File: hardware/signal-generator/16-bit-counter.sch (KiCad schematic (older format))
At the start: 8 parts, among them U1 74HC04, U13 74HC4040, U14 74HC4040, U2 74HC08, U3 74HC08, U4 74HC30

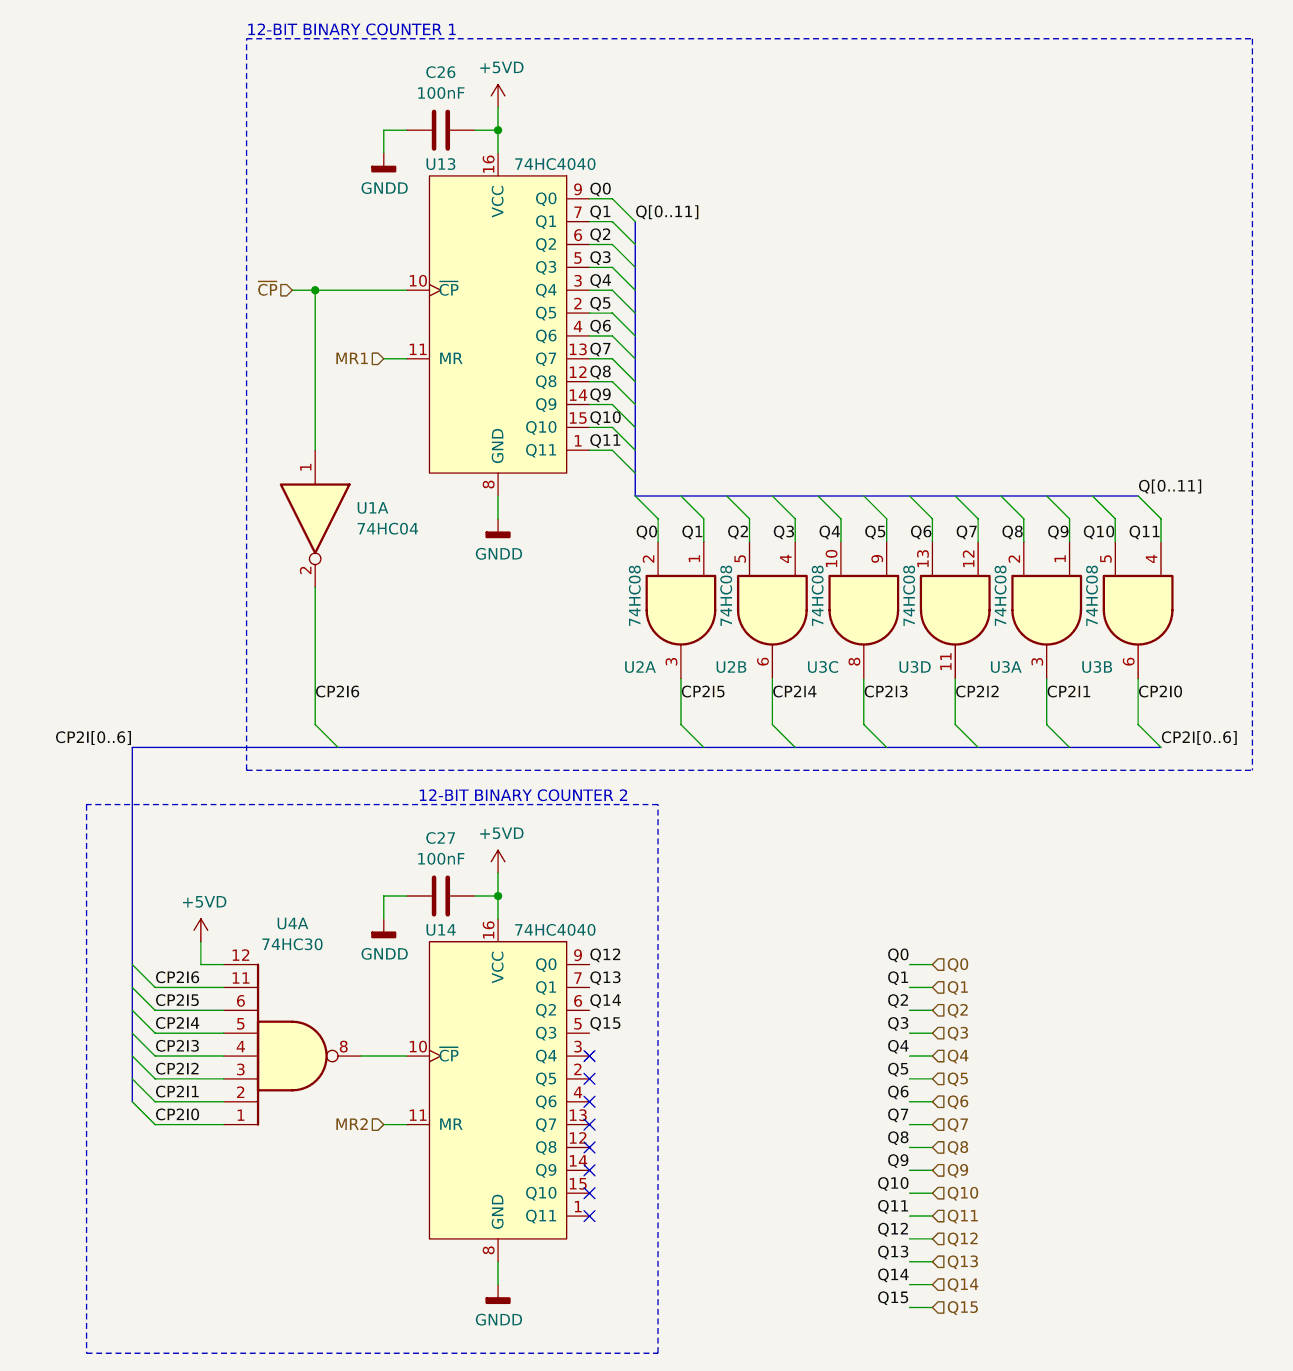
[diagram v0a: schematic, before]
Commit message: [Signal Generator] Change LCD backlight control method
The LCD's backlight was previously intended to be controlled via a
digital potentiometer. However, a much more elegant solution is to
control said backlight via PWM.

Also, removed the level shifter schematic sheet. The level shifters have been
moved to the TFT module's schematic sheet.
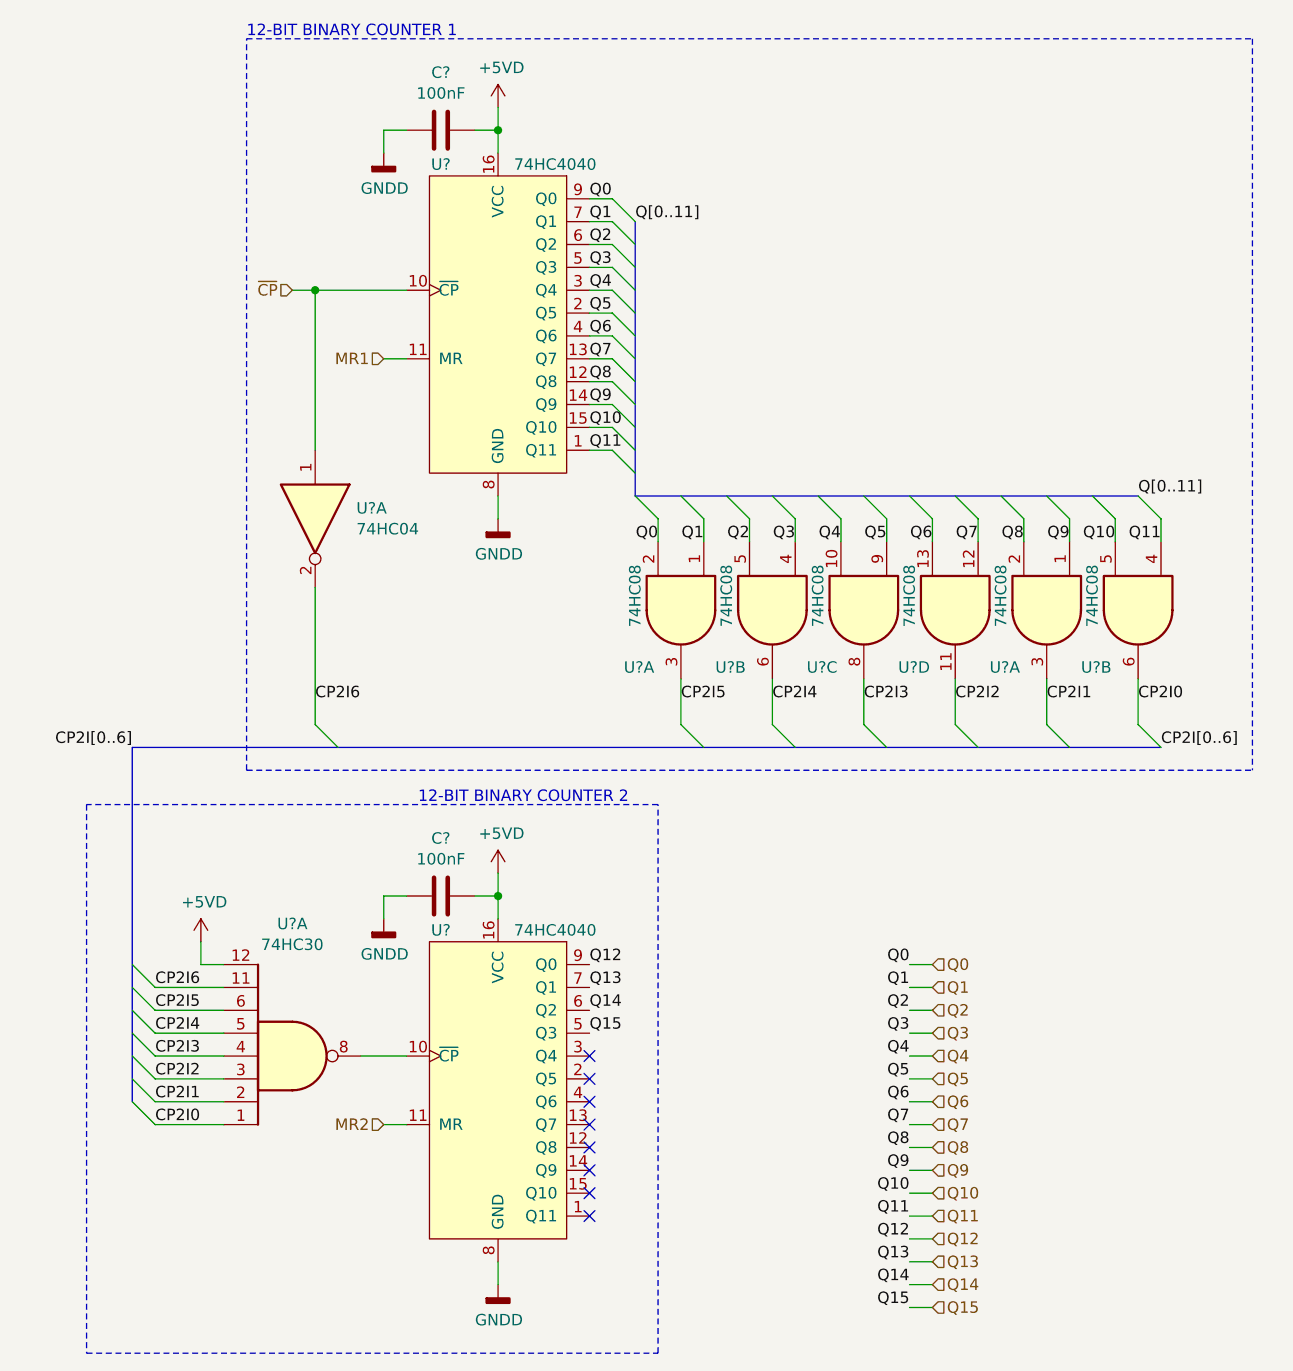
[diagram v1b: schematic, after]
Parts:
- renumbered C27 to C?, C26 to C?, U1 to U?, U13 to U?, U14 to U?, U4 to U?, U2 to U?, U3 to U?
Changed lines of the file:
@@
 $Descr A4 11693 8268
 encoding utf-8
-Sheet 3 6
+Sheet 3 5
 Title "Digital Function Generator v2 - DDS 16-bit counter"
 Date "2019-12-02"
@@
 	3650 5300 3850 5300
 $Comp
-L Device:C C27
+L Device:C C?
 U 1 1 5DBB7F3D
 P 4000 4600
-F 0 "C27" V 3748 4600 50  0000 C CNN
+F 0 "C?" V 3748 4600 50  0000 C CNN
 F 1 "100nF" V 3839 4600 50  0000 C CNN
 F 2 "Capacitors_SMD:C_0805_HandSoldering" H 4038 4450 50  0001 C CNN
@@
 	3750 4600 3750 4700
 $Comp
-L power:GNDD #PWR0172
+L power:GNDD #PWR?
 U 1 1 5DBB9690
 P 3750 4700
-F 0 "#PWR0172" H 3750 4450 50  0001 C CNN
+F 0 "#PWR?" H 3750 4450 50  0001 C CNN
 F 1 "GNDD" H 3754 4545 50  0000 C CNN
 F 2 "" H 3750 4700 50  0001 C CNN
@@
 Connection ~ 4250 4600
 $Comp
-L power:+5VD #PWR0173
+L power:+5VD #PWR?
 U 1 1 5DBB9DC1
 P 4250 4500
-F 0 "#PWR0173" H 4250 4350 50  0001 C CNN
+F 0 "#PWR?" H 4250 4350 50  0001 C CNN
 F 1 "+5VD" H 4265 4673 50  0000 C CNN
 F 2 "" H 4250 4500 50  0001 C CNN
@@
 $EndComp
 $Comp
-L Device:C C26
+L Device:C C?
 U 1 1 5DBBA88D
 P 4000 1250
-F 0 "C26" V 3748 1250 50  0000 C CNN
+F 0 "C?" V 3748 1250 50  0000 C CNN
 F 1 "100nF" V 3839 1250 50  0000 C CNN
 F 2 "Capacitors_SMD:C_0805_HandSoldering" H 4038 1100 50  0001 C CNN
@@
 	3750 1250 3750 1350
 $Comp
-L power:GNDD #PWR0174
+L power:GNDD #PWR?
 U 1 1 5DBBB94E
 P 3750 1350
-F 0 "#PWR0174" H 3750 1100 50  0001 C CNN
+F 0 "#PWR?" H 3750 1100 50  0001 C CNN
 F 1 "GNDD" H 3754 1195 50  0000 C CNN
 F 2 "" H 3750 1350 50  0001 C CNN
@@
 Connection ~ 4250 1250
 $Comp
-L power:+5VD #PWR0175
+L power:+5VD #PWR?
 U 1 1 5DBBC2D6
 P 4250 1150
-F 0 "#PWR0175" H 4250 1000 50  0001 C CNN
+F 0 "#PWR?" H 4250 1000 50  0001 C CNN
 F 1 "+5VD" H 4265 1323 50  0000 C CNN
 F 2 "" H 4250 1150 50  0001 C CNN
@@
 	4250 2850 4250 2950
 $Comp
-L power:GNDD #PWR0176
+L power:GNDD #PWR?
 U 1 1 5DBBD1F3
 P 4250 2950
-F 0 "#PWR0176" H 4250 2700 50  0001 C CNN
+F 0 "#PWR?" H 4250 2700 50  0001 C CNN
 F 1 "GNDD" H 4254 2795 50  0000 C CNN
 F 2 "" H 4250 2950 50  0001 C CNN
@@
 	4250 6200 4250 6300
 $Comp
-L power:GNDD #PWR0177
+L power:GNDD #PWR?
 U 1 1 5DBBE1A2
 P 4250 6300
-F 0 "#PWR0177" H 4250 6050 50  0001 C CNN
+F 0 "#PWR?" H 4250 6050 50  0001 C CNN
 F 1 "GNDD" H 4254 6145 50  0000 C CNN
 F 2 "" H 4250 6300 50  0001 C CNN
@@
 	2950 4900 2950 4800
 $Comp
-L power:+5VD #PWR0178
+L power:+5VD #PWR?
 U 1 1 5DBCA96D
 P 2950 4800
-F 0 "#PWR0178" H 2950 4650 50  0001 C CNN
+F 0 "#PWR?" H 2950 4650 50  0001 C CNN
 F 1 "+5VD" H 2965 4973 50  0000 C CNN
 F 2 "" H 2950 4800 50  0001 C CNN
@@
 12-BIT BINARY COUNTER 2
 $Comp
-L 74xx:74HC04 U1
+L 74xx:74HC04 U?
 U 1 1 5DBD607E
 P 3450 2950
-F 0 "U1" V 3404 3130 50  0000 L CNN
+F 0 "U?" V 3404 3130 50  0000 L CNN
 F 1 "74HC04" V 3495 3130 50  0000 L CNN
 F 2 "Housings_SOIC:SOIC-14_3.9x8.7mm_Pitch1.27mm" H 3450 2950 50  0001 C CNN
@@
 	3450 1950 3850 1950
 $Comp
-L ulib_MY_74xx:74HC4040 U13
+L ulib_MY_74xx:74HC4040 U?
 U 1 1 5DDE79E4
 P 4250 2100
-F 0 "U13" H 4000 2800 50  0000 C CNN
+F 0 "U?" H 4000 2800 50  0000 C CNN
 F 1 "74HC4040" H 4500 2800 50  0000 C CNN
 F 2 "Housings_SOIC:SOIC-16_3.9x9.9mm_Pitch1.27mm" H 4250 2050 50  0001 C CNN
@@
 $EndComp
 $Comp
-L ulib_MY_74xx:74HC4040 U14
+L ulib_MY_74xx:74HC4040 U?
 U 1 1 5DDE7D79
 P 4250 5450
-F 0 "U14" H 4000 6150 50  0000 C CNN
+F 0 "U?" H 4000 6150 50  0000 C CNN
 F 1 "74HC4040" H 4500 6150 50  0000 C CNN
 F 2 "Housings_SOIC:SOIC-16_3.9x9.9mm_Pitch1.27mm" H 4250 5400 50  0001 C CNN
@@
 $EndComp
 $Comp
-L ulib_MY_74xx:74HC30 U4
+L ulib_MY_74xx:74HC30 U?
 U 1 1 5DDE81EA
 P 3350 5300
-F 0 "U4" H 3350 4722 50  0000 C CNN
+F 0 "U?" H 3350 4722 50  0000 C CNN
 F 1 "74HC30" H 3350 4813 50  0000 C CNN
 F 2 "Housings_SOIC:SOIC-14_3.9x8.7mm_Pitch1.27mm" H 3350 5250 50  0001 C CNN
@@
 $EndComp
 $Comp
-L ulib_MY_74xx:74HC08 U2
+L ulib_MY_74xx:74HC08 U?
 U 1 1 5DDE88D1
 P 5050 3350
-F 0 "U2" V 5300 3100 50  0000 L CNN
+F 0 "U?" V 5300 3100 50  0000 L CNN
 F 1 "74HC08" H 4850 3150 50  0000 L CNN
 F 2 "Housings_SOIC:SOIC-14_3.9x8.7mm_Pitch1.27mm" H 5050 3300 50  0001 C CNN
@@
 $EndComp
 $Comp
-L ulib_MY_74xx:74HC08 U2
+L ulib_MY_74xx:74HC08 U?
 U 2 1 5DDE89F7
 P 5450 3350
-F 0 "U2" V 5700 3100 50  0000 L CNN
+F 0 "U?" V 5700 3100 50  0000 L CNN
 F 1 "74HC08" H 5250 3150 50  0000 L CNN
 F 2 "Housings_SOIC:SOIC-14_3.9x8.7mm_Pitch1.27mm" H 5450 3300 50  0001 C CNN
@@
 $EndComp
 $Comp
-L ulib_MY_74xx:74HC08 U3
+L ulib_MY_74xx:74HC08 U?
 U 3 1 5DDE8B26
 P 5850 3350
-F 0 "U3" V 6100 3100 50  0000 L CNN
+F 0 "U?" V 6100 3100 50  0000 L CNN
 F 1 "74HC08" H 5650 3150 50  0000 L CNN
 F 2 "Housings_SOIC:SOIC-14_3.9x8.7mm_Pitch1.27mm" H 5850 3300 50  0001 C CNN
@@
 $EndComp
 $Comp
-L ulib_MY_74xx:74HC08 U3
+L ulib_MY_74xx:74HC08 U?
 U 4 1 5DDE8C64
 P 6250 3350
-F 0 "U3" V 6500 3100 50  0000 L CNN
+F 0 "U?" V 6500 3100 50  0000 L CNN
 F 1 "74HC08" H 6050 3150 50  0000 L CNN
 F 2 "Housings_SOIC:SOIC-14_3.9x8.7mm_Pitch1.27mm" H 6250 3300 50  0001 C CNN
@@
 $EndComp
 $Comp
-L ulib_MY_74xx:74HC08 U3
+L ulib_MY_74xx:74HC08 U?
 U 1 1 5DDE8DB3
 P 6650 3350
-F 0 "U3" V 6900 3100 50  0000 L CNN
+F 0 "U?" V 6900 3100 50  0000 L CNN
 F 1 "74HC08" H 6450 3150 50  0000 L CNN
 F 2 "Housings_SOIC:SOIC-14_3.9x8.7mm_Pitch1.27mm" H 6650 3300 50  0001 C CNN
@@
 $EndComp
 $Comp
-L ulib_MY_74xx:74HC08 U3
+L ulib_MY_74xx:74HC08 U?
 U 2 1 5DDE8F14
 P 7050 3350
-F 0 "U3" V 7300 3100 50  0000 L CNN
+F 0 "U?" V 7300 3100 50  0000 L CNN
 F 1 "74HC08" H 6850 3150 50  0000 L CNN
 F 2 "Housings_SOIC:SOIC-14_3.9x8.7mm_Pitch1.27mm" H 7050 3300 50  0001 C CNN

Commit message: [Signal Generator] Finalize schematic
The electronic schematic is now finalized. All components have been
annotated. Furthermore, all components have an appropriate footprint
associated to them.
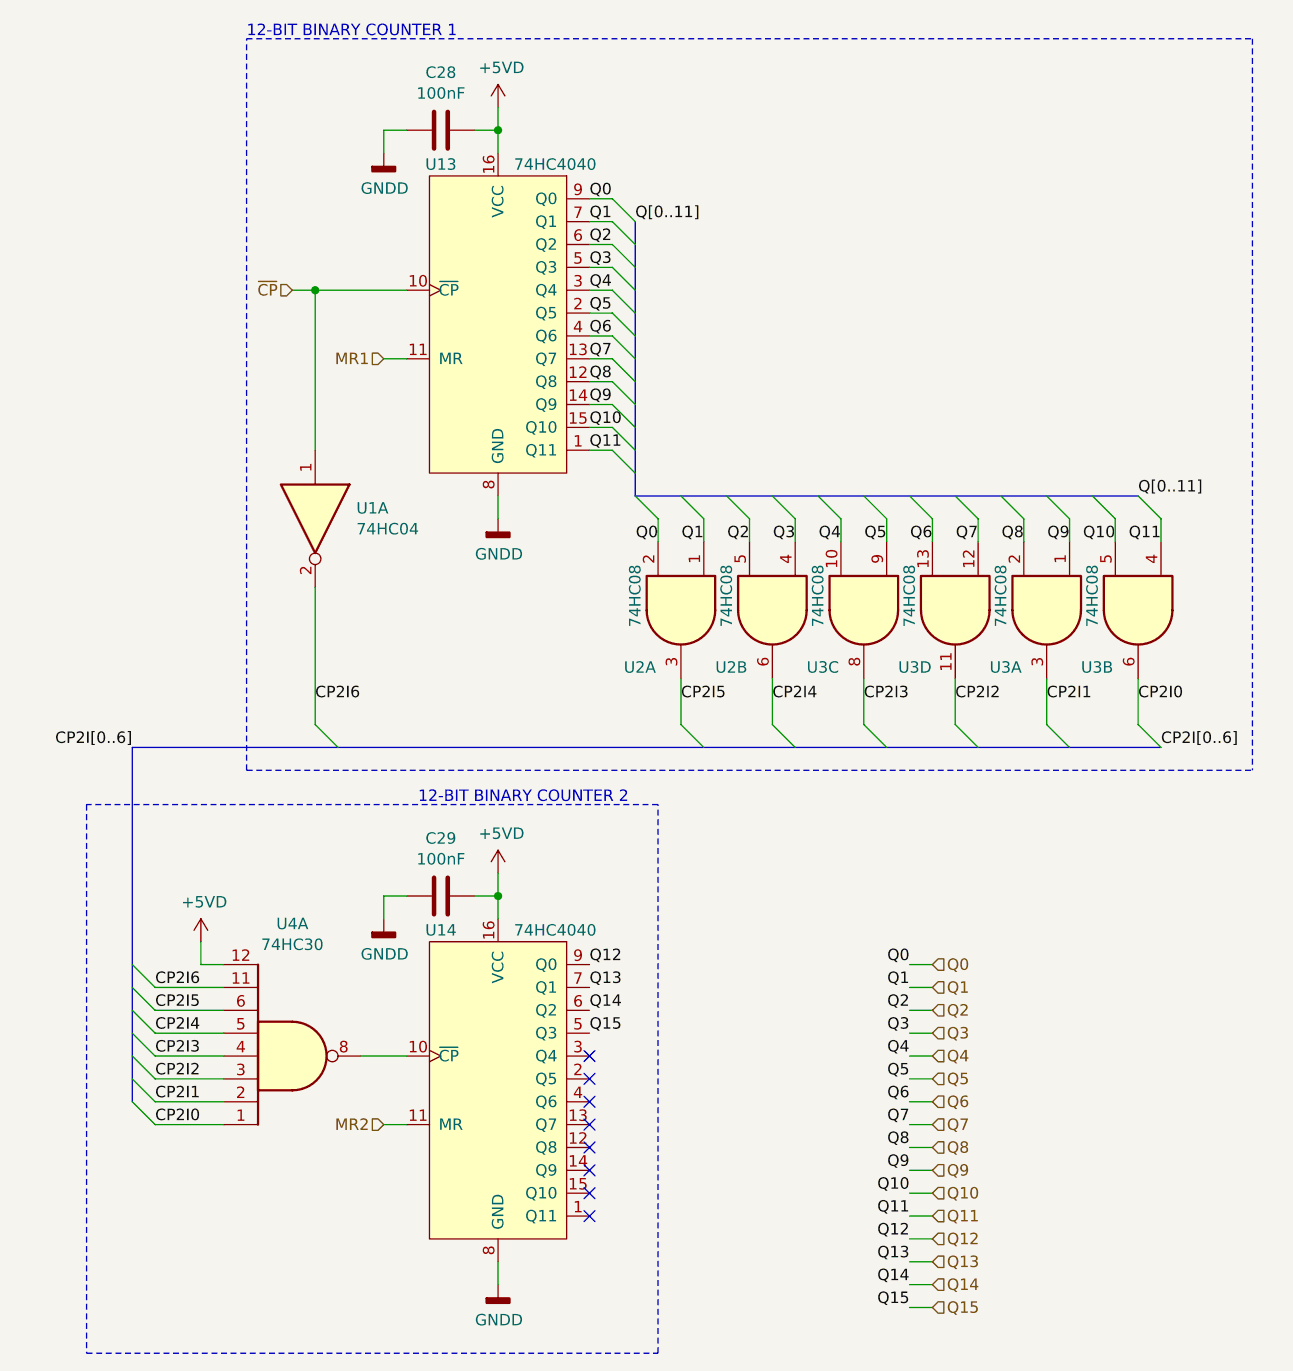
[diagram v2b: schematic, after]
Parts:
- gave numbers to parts that had none: 8
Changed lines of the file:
@@
 	3650 5300 3850 5300
 $Comp
-L Device:C C?
+L Device:C C29
 U 1 1 5DBB7F3D
 P 4000 4600
-F 0 "C?" V 3748 4600 50  0000 C CNN
+F 0 "C29" V 3748 4600 50  0000 C CNN
 F 1 "100nF" V 3839 4600 50  0000 C CNN
 F 2 "Capacitors_SMD:C_0805_HandSoldering" H 4038 4450 50  0001 C CNN
@@
 	3750 4600 3750 4700
 $Comp
-L power:GNDD #PWR?
+L power:GNDD #PWR077
 U 1 1 5DBB9690
 P 3750 4700
-F 0 "#PWR?" H 3750 4450 50  0001 C CNN
+F 0 "#PWR077" H 3750 4450 50  0001 C CNN
 F 1 "GNDD" H 3754 4545 50  0000 C CNN
 F 2 "" H 3750 4700 50  0001 C CNN
@@
 Connection ~ 4250 4600
 $Comp
-L power:+5VD #PWR?
+L power:+5VD #PWR080
 U 1 1 5DBB9DC1
 P 4250 4500
-F 0 "#PWR?" H 4250 4350 50  0001 C CNN
+F 0 "#PWR080" H 4250 4350 50  0001 C CNN
 F 1 "+5VD" H 4265 4673 50  0000 C CNN
 F 2 "" H 4250 4500 50  0001 C CNN
@@
 $EndComp
 $Comp
-L Device:C C?
+L Device:C C28
 U 1 1 5DBBA88D
 P 4000 1250
-F 0 "C?" V 3748 1250 50  0000 C CNN
+F 0 "C28" V 3748 1250 50  0000 C CNN
 F 1 "100nF" V 3839 1250 50  0000 C CNN
 F 2 "Capacitors_SMD:C_0805_HandSoldering" H 4038 1100 50  0001 C CNN
@@
 	3750 1250 3750 1350
 $Comp
-L power:GNDD #PWR?
+L power:GNDD #PWR076
 U 1 1 5DBBB94E
 P 3750 1350
-F 0 "#PWR?" H 3750 1100 50  0001 C CNN
+F 0 "#PWR076" H 3750 1100 50  0001 C CNN
 F 1 "GNDD" H 3754 1195 50  0000 C CNN
 F 2 "" H 3750 1350 50  0001 C CNN
@@
 Connection ~ 4250 1250
 $Comp
-L power:+5VD #PWR?
+L power:+5VD #PWR078
 U 1 1 5DBBC2D6
 P 4250 1150
-F 0 "#PWR?" H 4250 1000 50  0001 C CNN
+F 0 "#PWR078" H 4250 1000 50  0001 C CNN
 F 1 "+5VD" H 4265 1323 50  0000 C CNN
 F 2 "" H 4250 1150 50  0001 C CNN
@@
 	4250 2850 4250 2950
 $Comp
-L power:GNDD #PWR?
+L power:GNDD #PWR079
 U 1 1 5DBBD1F3
 P 4250 2950
-F 0 "#PWR?" H 4250 2700 50  0001 C CNN
+F 0 "#PWR079" H 4250 2700 50  0001 C CNN
 F 1 "GNDD" H 4254 2795 50  0000 C CNN
 F 2 "" H 4250 2950 50  0001 C CNN
@@
 	4250 6200 4250 6300
 $Comp
-L power:GNDD #PWR?
+L power:GNDD #PWR081
 U 1 1 5DBBE1A2
 P 4250 6300
-F 0 "#PWR?" H 4250 6050 50  0001 C CNN
+F 0 "#PWR081" H 4250 6050 50  0001 C CNN
 F 1 "GNDD" H 4254 6145 50  0000 C CNN
 F 2 "" H 4250 6300 50  0001 C CNN
@@
 	2950 4900 2950 4800
 $Comp
-L power:+5VD #PWR?
+L power:+5VD #PWR075
 U 1 1 5DBCA96D
 P 2950 4800
-F 0 "#PWR?" H 2950 4650 50  0001 C CNN
+F 0 "#PWR075" H 2950 4650 50  0001 C CNN
 F 1 "+5VD" H 2965 4973 50  0000 C CNN
 F 2 "" H 2950 4800 50  0001 C CNN
@@
 12-BIT BINARY COUNTER 2
 $Comp
-L 74xx:74HC04 U?
+L 74xx:74HC04 U1
 U 1 1 5DBD607E
 P 3450 2950
-F 0 "U?" V 3404 3130 50  0000 L CNN
+F 0 "U1" V 3404 3130 50  0000 L CNN
 F 1 "74HC04" V 3495 3130 50  0000 L CNN
 F 2 "Housings_SOIC:SOIC-14_3.9x8.7mm_Pitch1.27mm" H 3450 2950 50  0001 C CNN
@@
 	3450 1950 3850 1950
 $Comp
-L ulib_MY_74xx:74HC4040 U?
+L ulib_MY_74xx:74HC4040 U13
 U 1 1 5DDE79E4
 P 4250 2100
-F 0 "U?" H 4000 2800 50  0000 C CNN
+F 0 "U13" H 4000 2800 50  0000 C CNN
 F 1 "74HC4040" H 4500 2800 50  0000 C CNN
 F 2 "Housings_SOIC:SOIC-16_3.9x9.9mm_Pitch1.27mm" H 4250 2050 50  0001 C CNN
@@
 $EndComp
 $Comp
-L ulib_MY_74xx:74HC4040 U?
+L ulib_MY_74xx:74HC4040 U14
 U 1 1 5DDE7D79
 P 4250 5450
-F 0 "U?" H 4000 6150 50  0000 C CNN
+F 0 "U14" H 4000 6150 50  0000 C CNN
 F 1 "74HC4040" H 4500 6150 50  0000 C CNN
 F 2 "Housings_SOIC:SOIC-16_3.9x9.9mm_Pitch1.27mm" H 4250 5400 50  0001 C CNN
@@
 $EndComp
 $Comp
-L ulib_MY_74xx:74HC30 U?
+L ulib_MY_74xx:74HC30 U4
 U 1 1 5DDE81EA
 P 3350 5300
-F 0 "U?" H 3350 4722 50  0000 C CNN
+F 0 "U4" H 3350 4722 50  0000 C CNN
 F 1 "74HC30" H 3350 4813 50  0000 C CNN
 F 2 "Housings_SOIC:SOIC-14_3.9x8.7mm_Pitch1.27mm" H 3350 5250 50  0001 C CNN
@@
 $EndComp
 $Comp
-L ulib_MY_74xx:74HC08 U?
+L ulib_MY_74xx:74HC08 U2
 U 1 1 5DDE88D1
 P 5050 3350
-F 0 "U?" V 5300 3100 50  0000 L CNN
+F 0 "U2" V 5300 3100 50  0000 L CNN
 F 1 "74HC08" H 4850 3150 50  0000 L CNN
 F 2 "Housings_SOIC:SOIC-14_3.9x8.7mm_Pitch1.27mm" H 5050 3300 50  0001 C CNN
@@
 $EndComp
 $Comp
-L ulib_MY_74xx:74HC08 U?
+L ulib_MY_74xx:74HC08 U2
 U 2 1 5DDE89F7
 P 5450 3350
-F 0 "U?" V 5700 3100 50  0000 L CNN
+F 0 "U2" V 5700 3100 50  0000 L CNN
 F 1 "74HC08" H 5250 3150 50  0000 L CNN
 F 2 "Housings_SOIC:SOIC-14_3.9x8.7mm_Pitch1.27mm" H 5450 3300 50  0001 C CNN
@@
 $EndComp
 $Comp
-L ulib_MY_74xx:74HC08 U?
+L ulib_MY_74xx:74HC08 U3
 U 3 1 5DDE8B26
 P 5850 3350
-F 0 "U?" V 6100 3100 50  0000 L CNN
+F 0 "U3" V 6100 3100 50  0000 L CNN
 F 1 "74HC08" H 5650 3150 50  0000 L CNN
 F 2 "Housings_SOIC:SOIC-14_3.9x8.7mm_Pitch1.27mm" H 5850 3300 50  0001 C CNN
@@
 $EndComp
 $Comp
-L ulib_MY_74xx:74HC08 U?
+L ulib_MY_74xx:74HC08 U3
 U 4 1 5DDE8C64
 P 6250 3350
-F 0 "U?" V 6500 3100 50  0000 L CNN
+F 0 "U3" V 6500 3100 50  0000 L CNN
 F 1 "74HC08" H 6050 3150 50  0000 L CNN
 F 2 "Housings_SOIC:SOIC-14_3.9x8.7mm_Pitch1.27mm" H 6250 3300 50  0001 C CNN
@@
 $EndComp
 $Comp
-L ulib_MY_74xx:74HC08 U?
+L ulib_MY_74xx:74HC08 U3
 U 1 1 5DDE8DB3
 P 6650 3350
-F 0 "U?" V 6900 3100 50  0000 L CNN
+F 0 "U3" V 6900 3100 50  0000 L CNN
 F 1 "74HC08" H 6450 3150 50  0000 L CNN
 F 2 "Housings_SOIC:SOIC-14_3.9x8.7mm_Pitch1.27mm" H 6650 3300 50  0001 C CNN
@@
 $EndComp
 $Comp
-L ulib_MY_74xx:74HC08 U?
+L ulib_MY_74xx:74HC08 U3
 U 2 1 5DDE8F14
 P 7050 3350
-F 0 "U?" V 7300 3100 50  0000 L CNN
+F 0 "U3" V 7300 3100 50  0000 L CNN
 F 1 "74HC08" H 6850 3150 50  0000 L CNN
 F 2 "Housings_SOIC:SOIC-14_3.9x8.7mm_Pitch1.27mm" H 7050 3300 50  0001 C CNN
